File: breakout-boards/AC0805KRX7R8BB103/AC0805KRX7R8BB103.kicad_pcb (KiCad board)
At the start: 2 copper layers, 14 parts, among them J1 Conn_01x12, J2 Conn_01x12

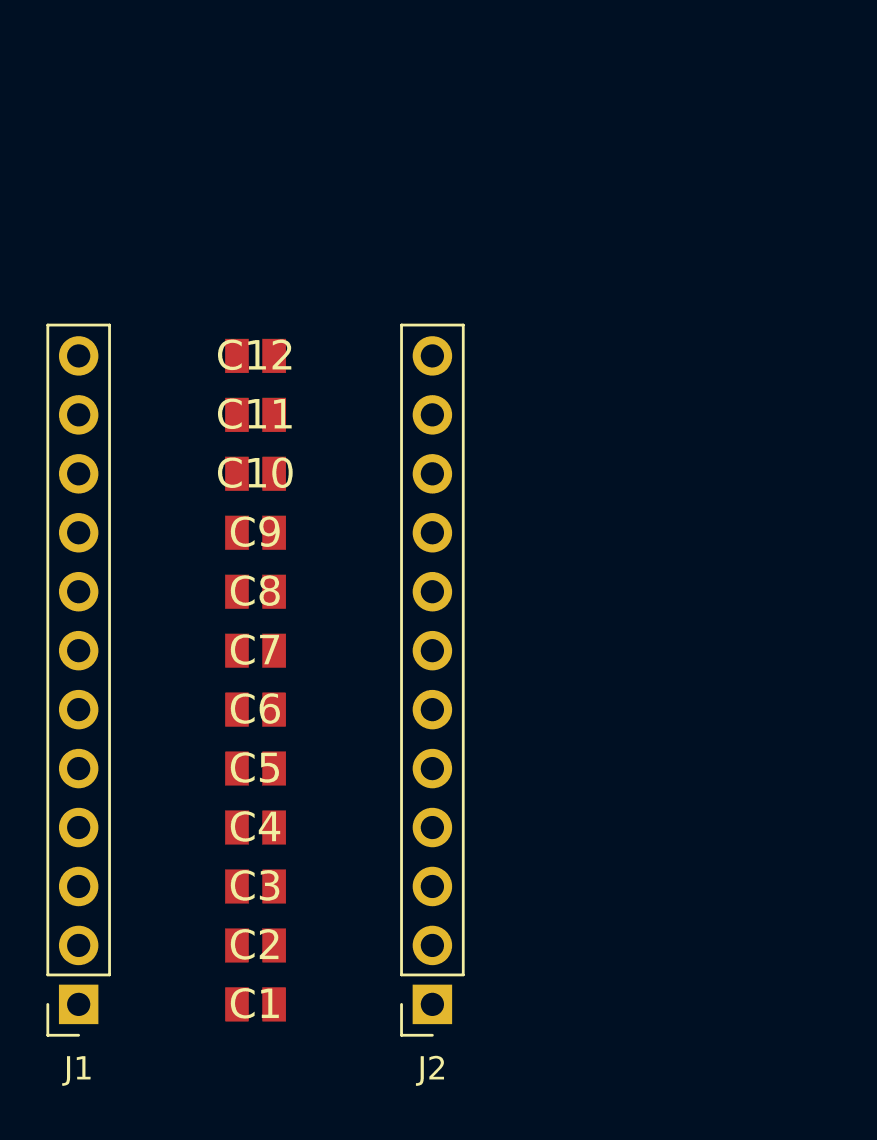
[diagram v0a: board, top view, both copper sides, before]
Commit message: feat: create footprint for capacitor breakout board
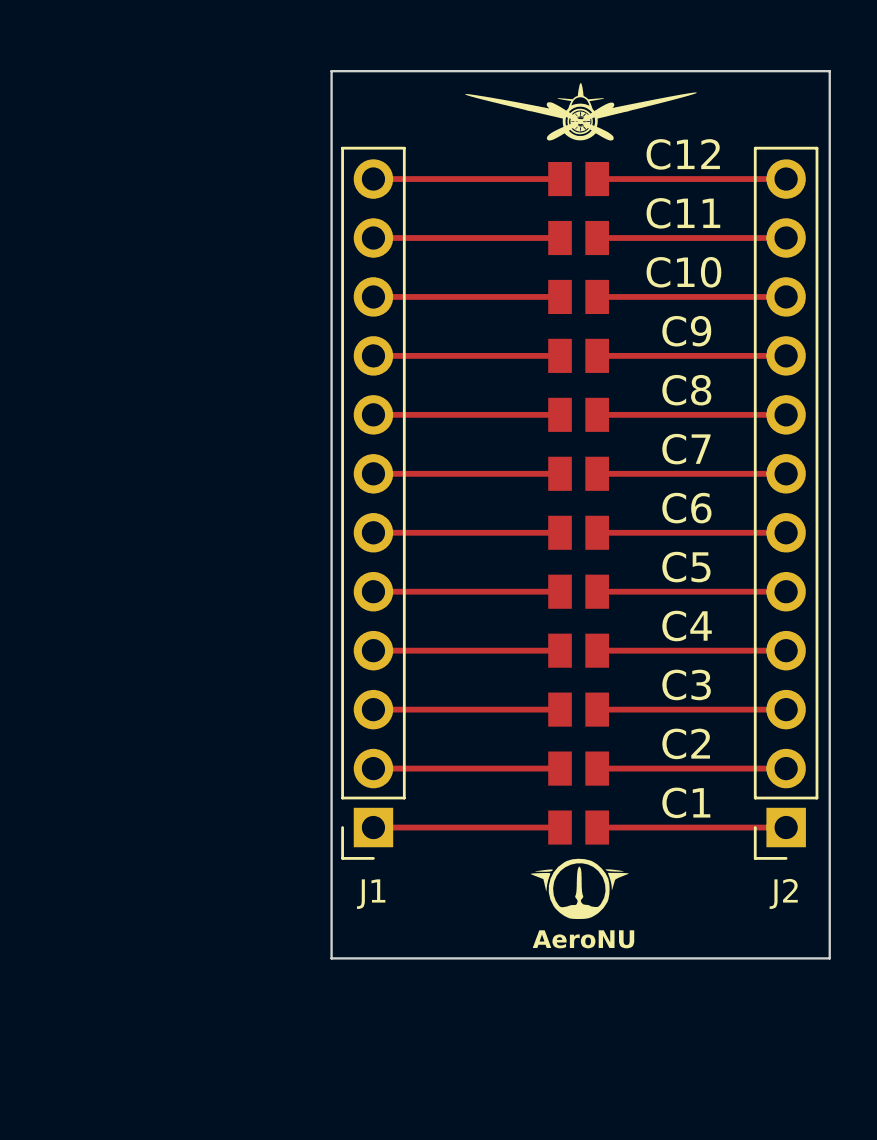
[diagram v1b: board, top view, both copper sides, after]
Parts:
- added AeroNU: LOGO, FixedWing:AeroNU - Logo (Smol), F.Cu at (161.4, 109.6)
- added FixedWing: LOGO, FixedWing:FixedWing - Logo (Smol), F.Cu at (161.4, 74.0)
- moved J2 17.0 mm to (170.2, 104.1)
- moved C1 15.9 mm to (161.2, 104.1), turned to 0 degrees
- moved C10 15.9 mm to (161.2, 81.3), turned to 0 degrees
- moved C11 15.9 mm to (161.2, 78.7), turned to 0 degrees
- moved C2 15.9 mm to (161.2, 101.6), turned to 0 degrees
- moved C3 15.9 mm to (161.2, 99.1), turned to 0 degrees
- moved C4 15.9 mm to (161.2, 96.5), turned to 0 degrees
- moved C6 15.9 mm to (161.2, 91.4), turned to 0 degrees
- moved C8 15.9 mm to (161.2, 86.4), turned to 0 degrees
- moved C9 15.9 mm to (161.2, 83.8), turned to 0 degrees
- moved C12 15.9 mm to (161.2, 76.2), turned to 0 degrees
- moved C5 15.9 mm to (161.2, 94.0), turned to 0 degrees
- moved C7 15.9 mm to (161.2, 88.9), turned to 0 degrees
- moved J1 14.8 mm to (152.4, 104.1)
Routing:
- net Net-(J2-Pin_9): track 0.00 -> 8.25 mm
- net Net-(J2-Pin_8): track 0.00 -> 8.25 mm
- net Net-(J2-Pin_7): track 0.00 -> 8.25 mm
- net Net-(J2-Pin_6): track 0.00 -> 8.25 mm
- net Net-(J2-Pin_5): track 0.00 -> 8.25 mm
- net Net-(J2-Pin_4): track 0.00 -> 8.25 mm
- net Net-(J2-Pin_3): track 0.00 -> 8.25 mm
- net Net-(J2-Pin_2): track 0.00 -> 8.25 mm
- net Net-(J2-Pin_12): track 0.00 -> 8.25 mm
- net Net-(J2-Pin_11): track 0.00 -> 8.25 mm
- net Net-(J2-Pin_10): track 0.00 -> 8.25 mm
- net Net-(J2-Pin_1): track 0.00 -> 8.25 mm
- net Net-(J1-Pin_9): track 0.00 -> 7.92 mm
- net Net-(J1-Pin_8): track 0.00 -> 7.92 mm
- net Net-(J1-Pin_7): track 0.00 -> 7.92 mm
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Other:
- board outline added: 21.5 x 38.2 mm
- board text added: "AeroNU"
- board text added: "Designed By Ephram CJ and Matthew F"

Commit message: feat: create capacitor board panel
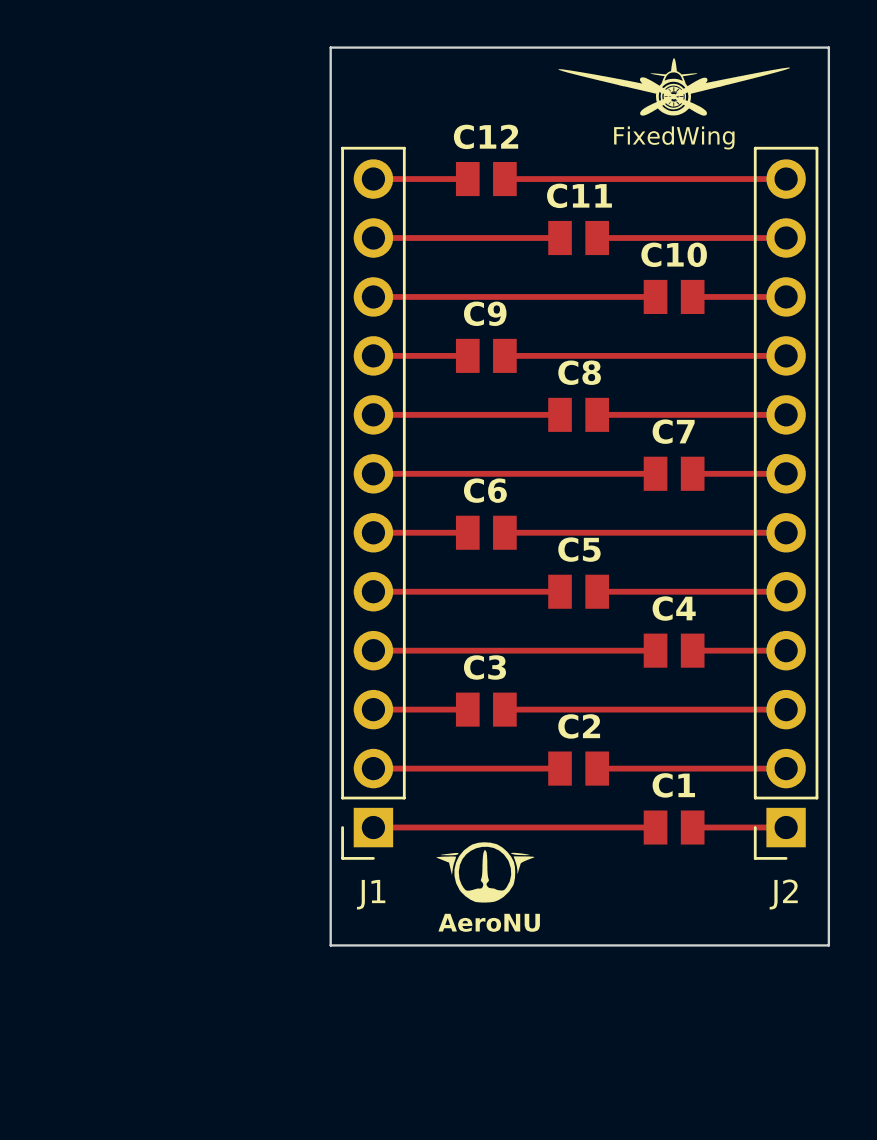
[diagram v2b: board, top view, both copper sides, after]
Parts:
- moved FixedWing 4.22 mm to (165.4, 72.6)
- moved AeroNU 4.13 mm to (157.3, 108.8)
- moved C1 4.11 mm to (165.4, 104.1)
- moved C10 4.11 mm to (165.4, 81.3)
- moved C4 4.11 mm to (165.4, 96.5)
- moved C7 4.11 mm to (165.4, 88.9)
- moved C12 3.98 mm to (157.3, 76.2)
- moved C3 3.98 mm to (157.3, 99.1)
- moved C6 3.98 mm to (157.3, 91.4)
- moved C9 3.98 mm to (157.3, 83.8)
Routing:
- net Net-(J1-Pin_7): track 7.92 -> 12.2 mm
- net Net-(J1-Pin_4): track 7.92 -> 12.2 mm
- net Net-(J1-Pin_10): track 7.92 -> 12.2 mm
- net Net-(J1-Pin_1): track 7.92 -> 12.2 mm
- net Net-(J2-Pin_7): track 8.25 -> 4.03 mm
- net Net-(J2-Pin_4): track 8.25 -> 4.03 mm
- net Net-(J2-Pin_10): track 8.25 -> 4.03 mm
- net Net-(J2-Pin_1): track 8.25 -> 4.03 mm
- net Net-(J2-Pin_9): track 8.25 -> 12.1 mm
- net Net-(J2-Pin_6): track 8.25 -> 12.1 mm
- net Net-(J2-Pin_3): track 8.25 -> 12.1 mm
- net Net-(J2-Pin_12): track 8.25 -> 12.1 mm
- net Net-(J1-Pin_9): track 7.92 -> 4.06 mm
- net Net-(J1-Pin_6): track 7.92 -> 4.06 mm
- net Net-(J1-Pin_3): track 7.92 -> 4.06 mm
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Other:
- board size 21.5 x 38.2 mm -> 21.5 x 38.7 mm

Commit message: feat: add fillets to all boards
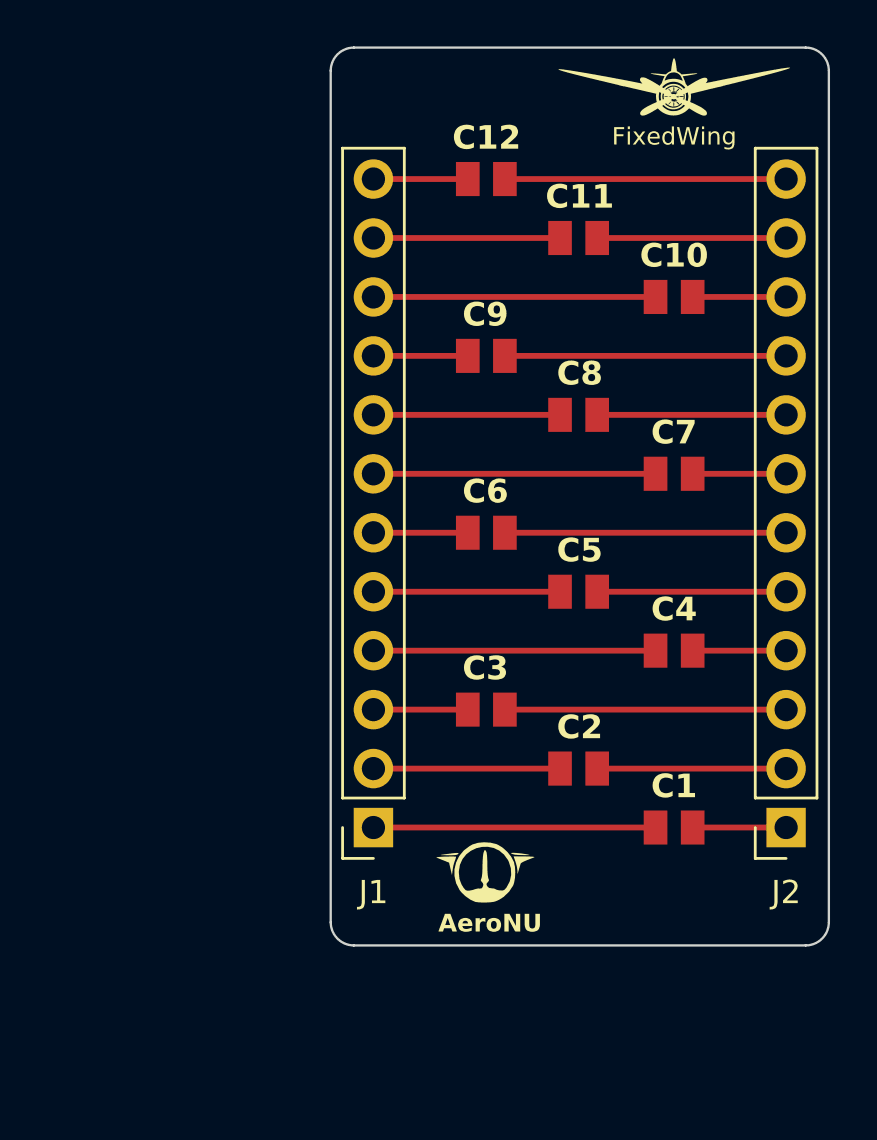
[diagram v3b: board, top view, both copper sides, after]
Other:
- outline, holes or cut-outs redrawn
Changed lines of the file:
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@@
       (outputformat 1)
       (mirror false)
-      (drillshape 1)
+      (drillshape 0)
       (scaleselection 1)
       (outputdirectory "")
@@
       (stroke (width 0) (type solid)) (fill solid) (layer "F.SilkS"))
   )
-  (gr_rect (start 150.5585 70.5358) (end 172.0215 109.22)
-    (stroke (width 0.1) (type default)) (fill none) (layer "Edge.Cuts"))
+  (gr_arc (start 150.5585 71.5358) (mid 150.851393 70.828693) (end 151.5585 70.5358)
+    (stroke (width 0.1) (type default)) (layer "Edge.Cuts"))
+  (gr_arc (start 172.0215 108.22) (mid 171.728607 108.927107) (end 171.0215 109.22)
+    (stroke (width 0.1) (type default)) (layer "Edge.Cuts"))
+  (gr_line (start 171.0215 109.22) (end 151.5585 109.22)
+    (stroke (width 0.1) (type default)) (layer "Edge.Cuts"))
+  (gr_arc (start 171.0215 70.5358) (mid 171.728607 70.828693) (end 172.0215 71.5358)
+    (stroke (width 0.1) (type default)) (layer "Edge.Cuts"))
+  (gr_line (start 150.5585 108.22) (end 150.5585 71.5358)
+    (stroke (width 0.1) (type default)) (layer "Edge.Cuts"))
+  (gr_arc (start 151.5585 109.22) (mid 150.851393 108.927107) (end 150.5585 108.22)
+    (stroke (width 0.1) (type default)) (layer "Edge.Cuts"))
+  (gr_line (start 172.0215 71.5358) (end 172.0215 108.22)
+    (stroke (width 0.1) (type default)) (layer "Edge.Cuts"))
+  (gr_line (start 151.5585 70.5358) (end 171.0215 70.5358)
+    (stroke (width 0.1) (type default)) (layer "Edge.Cuts"))
   (gr_text "Designed By\nEphram CJ and Matthew F" (at 161.3916 108.5596) (layer "B.SilkS")
     (effects (font (size 0.762 0.762) (thickness 0.127) bold) (justify bottom mirror))
